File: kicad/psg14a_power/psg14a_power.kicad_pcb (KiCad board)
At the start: 2 copper layers, 12 parts, among them J1 Power, J2 In, J3 Out, Q1 IRF9Z24N

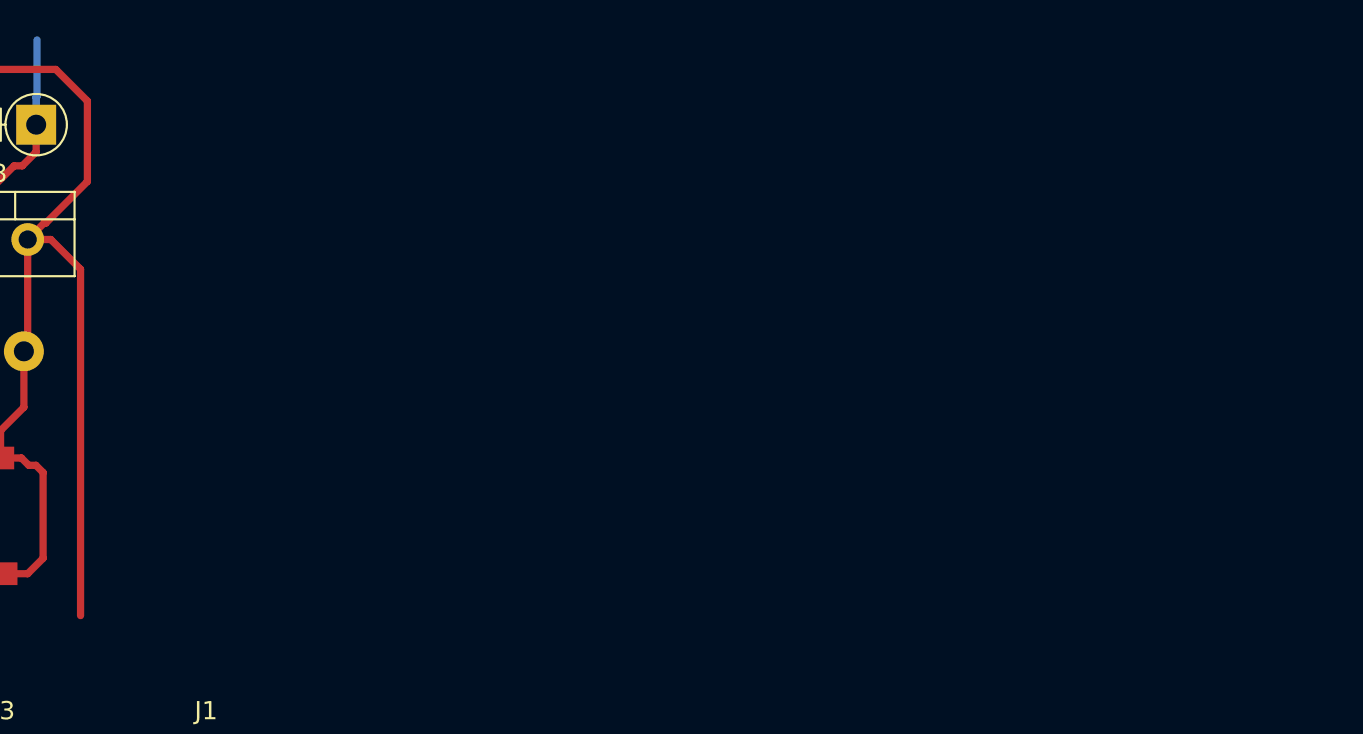
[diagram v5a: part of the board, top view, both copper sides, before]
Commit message: [psg14a_power] New layout
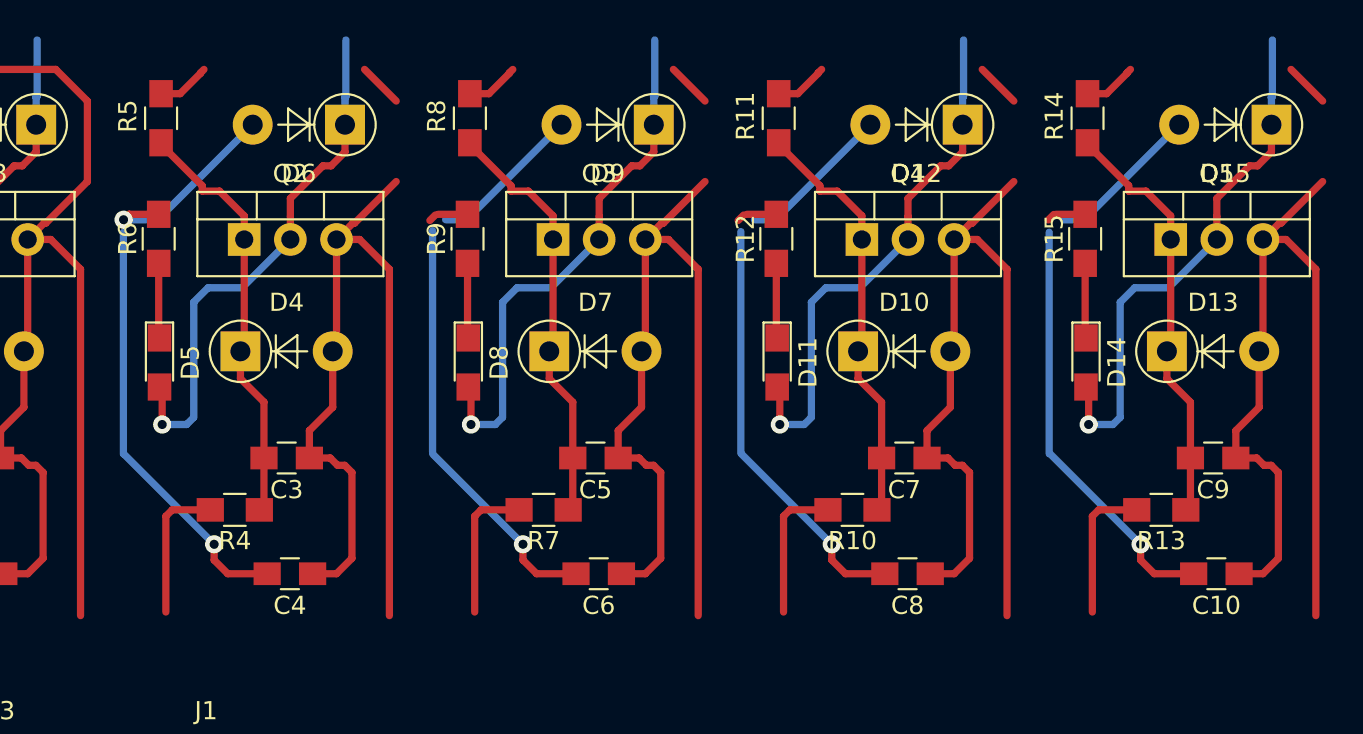
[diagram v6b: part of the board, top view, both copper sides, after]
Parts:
- added C10: 1uF 50V, Capacitors_SMD:C_0805_HandSoldering, F.Cu at (102.6, 56.2)
- added C3: 10nF, Capacitors_SMD:C_0805_HandSoldering, F.Cu at (51.4, 49.8)
- added C4: 1uF 50V, Capacitors_SMD:C_0805_HandSoldering, F.Cu at (51.6, 56.2)
- added C5: 10nF, Capacitors_SMD:C_0805_HandSoldering, F.Cu at (68.4, 49.8)
- added C6: 1uF 50V, Capacitors_SMD:C_0805_HandSoldering, F.Cu at (68.6, 56.2)
- added C7: 10nF, Capacitors_SMD:C_0805_HandSoldering, F.Cu at (85.4, 49.8)
- added C8: 1uF 50V, Capacitors_SMD:C_0805_HandSoldering, F.Cu at (85.6, 56.2)
- added C9: 10nF, Capacitors_SMD:C_0805_HandSoldering, F.Cu at (102.4, 49.8)
- added D10: BZX85_C12, Diodes_THT:D_DO-41_SOD81_P5.08mm_Vertical_AnodeUp, F.Cu at (82.8, 43.9)
- added D11: green, LEDs:LED_0805_HandSoldering, F.Cu at (78.4, 44.6)
- added D12: UF4007, Diodes_THT:D_DO-41_SOD81_P5.08mm_Vertical_AnodeUp, F.Cu at (88.6, 31.5)
- added D13: BZX85_C12, Diodes_THT:D_DO-41_SOD81_P5.08mm_Vertical_AnodeUp, F.Cu at (99.8, 43.9)
- added D14: green, LEDs:LED_0805_HandSoldering, F.Cu at (95.4, 44.6)
- added D15: UF4007, Diodes_THT:D_DO-41_SOD81_P5.08mm_Vertical_AnodeUp, F.Cu at (105.6, 31.5)
- added D4: BZX85_C12, Diodes_THT:D_DO-41_SOD81_P5.08mm_Vertical_AnodeUp, F.Cu at (48.8, 43.9)
- added D5: green, LEDs:LED_0805_HandSoldering, F.Cu at (44.4, 44.6)
- added D6: UF4007, Diodes_THT:D_DO-41_SOD81_P5.08mm_Vertical_AnodeUp, F.Cu at (54.6, 31.5)
- added D7: BZX85_C12, Diodes_THT:D_DO-41_SOD81_P5.08mm_Vertical_AnodeUp, F.Cu at (65.8, 43.9)
- added D8: green, LEDs:LED_0805_HandSoldering, F.Cu at (61.4, 44.6)
- added D9: UF4007, Diodes_THT:D_DO-41_SOD81_P5.08mm_Vertical_AnodeUp, F.Cu at (71.6, 31.5)
- added Q2: IRF9Z24N, TO_SOT_Packages_THT:TO-220-3_Vertical, F.Cu at (49.0, 37.8)
- added Q3: IRF9Z24N, TO_SOT_Packages_THT:TO-220-3_Vertical, F.Cu at (66.0, 37.8)
- added Q4: IRF9Z24N, TO_SOT_Packages_THT:TO-220-3_Vertical, F.Cu at (83.0, 37.8)
- added Q5: IRF9Z24N, TO_SOT_Packages_THT:TO-220-3_Vertical, F.Cu at (100.0, 37.8)
- added R10: 10K, Resistors_SMD:R_0805_HandSoldering, F.Cu at (82.5, 52.7)
- added R11: 10K, Resistors_SMD:R_0805_HandSoldering, F.Cu at (78.5, 31.1)
- added R12: 5k1, Resistors_SMD:R_0805_HandSoldering, F.Cu at (78.3, 37.7)
- added R13: 10K, Resistors_SMD:R_0805_HandSoldering, F.Cu at (99.5, 52.7)
- added R14: 10K, Resistors_SMD:R_0805_HandSoldering, F.Cu at (95.5, 31.1)
- added R15: 5k1, Resistors_SMD:R_0805_HandSoldering, F.Cu at (95.3, 37.7)
- added R4: 10K, Resistors_SMD:R_0805_HandSoldering, F.Cu at (48.5, 52.7)
- added R5: 10K, Resistors_SMD:R_0805_HandSoldering, F.Cu at (44.5, 31.1)
- added R6: 5k1, Resistors_SMD:R_0805_HandSoldering, F.Cu at (44.3, 37.7)
- added R7: 10K, Resistors_SMD:R_0805_HandSoldering, F.Cu at (65.5, 52.7)
- added R8: 10K, Resistors_SMD:R_0805_HandSoldering, F.Cu at (61.5, 31.1)
- added R9: 5k1, Resistors_SMD:R_0805_HandSoldering, F.Cu at (61.3, 37.7)
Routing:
- net /+24V: track 68.5 -> 289.4 mm
- net /GND: track 35.3 -> 171.7 mm, vias 2 -> 7
- net /Out3: track 0.00 -> 29.7 mm, vias 0 -> 1
- net /Out5: track 0.00 -> 29.7 mm, vias 0 -> 1
- net /Out4: track 0.00 -> 29.7 mm, vias 0 -> 1
- net /Out2: track 0.00 -> 29.7 mm, vias 0 -> 1
- net Net-(C3-Pad2): track 0.00 -> 23.4 mm
- net Net-(C9-Pad2): track 0.00 -> 23.4 mm
- net Net-(C7-Pad2): track 0.00 -> 23.4 mm
- net Net-(C5-Pad2): track 0.00 -> 23.4 mm
- net /In3: track 0.00 -> 7.86 mm
- net /In5: track 0.00 -> 7.86 mm
- net /In4: track 0.00 -> 7.86 mm
- net /In2: track 0.00 -> 7.86 mm
- net Net-(D14-Pad1): track 0.00 -> 4.13 mm
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
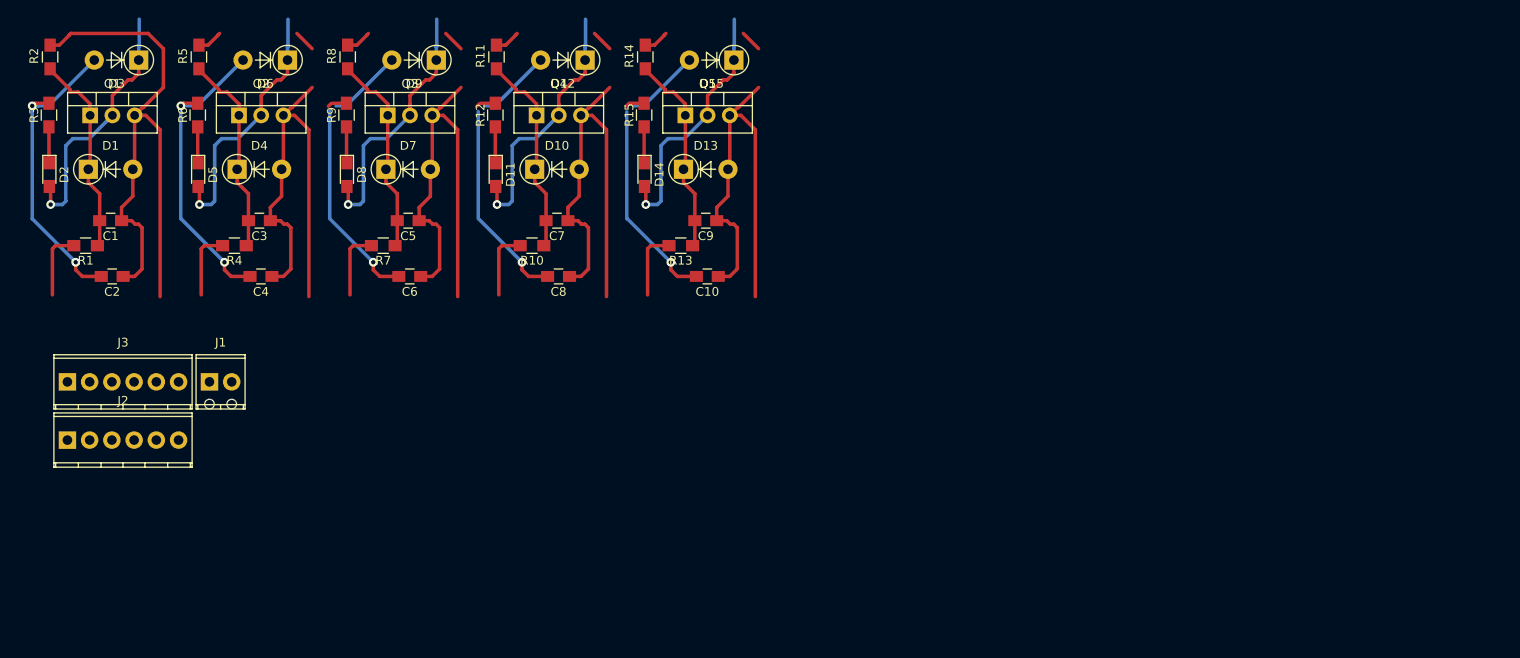
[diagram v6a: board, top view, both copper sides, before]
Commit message: [psg14a_power] New layout again
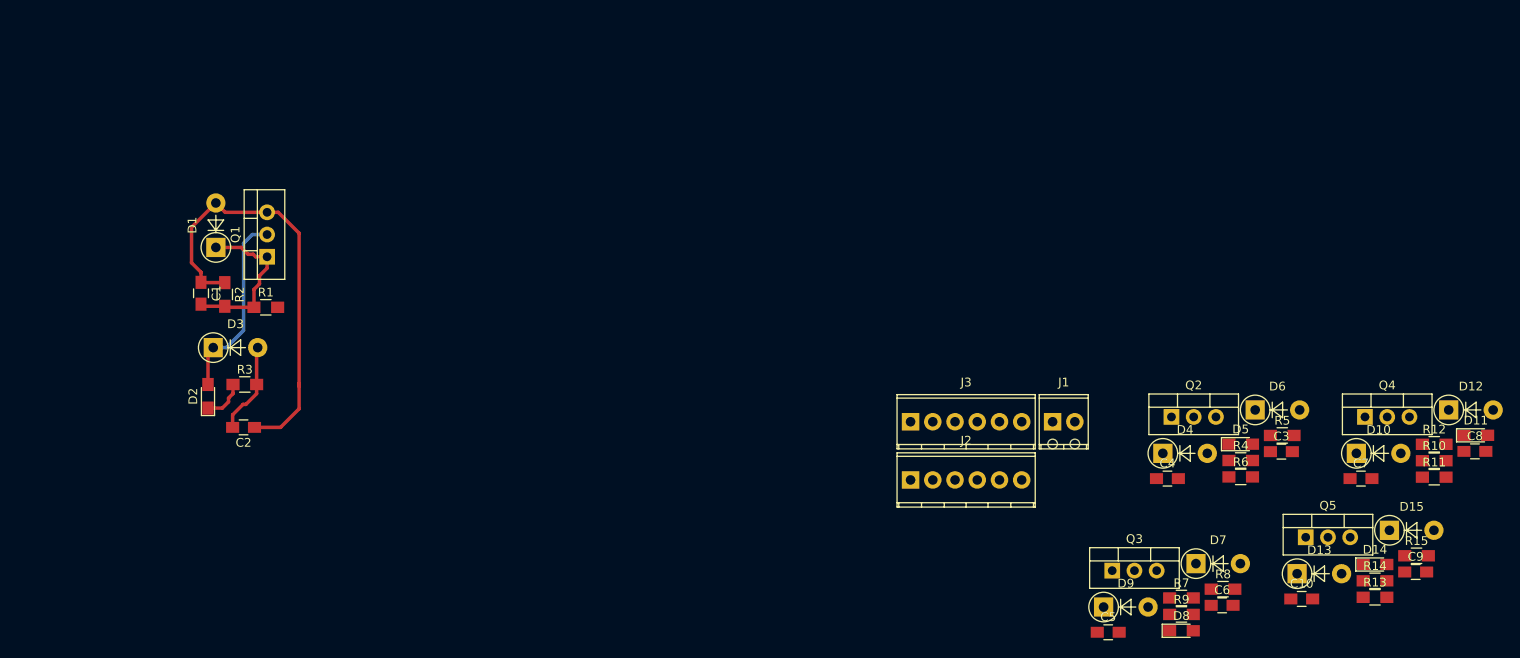
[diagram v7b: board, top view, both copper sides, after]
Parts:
- moved R5 131.1 mm to (168.3, 74.4), turned to 0 degrees
- moved R6 126.1 mm to (163.5, 79.1), turned to 0 degrees
- moved D5 123.0 mm to (163.5, 75.3), turned to 0 degrees
- moved C3 119.7 mm to (168.2, 76.2), turned to 0 degrees
- moved D6 117.6 mm to (165.2, 71.4), turned to 0 degrees
- moved R4 117.6 mm to (163.5, 77.2), turned to 0 degrees
- moved R11 117.4 mm to (185.6, 79.1), turned to 0 degrees
- moved R8 117.0 mm to (161.5, 91.9), turned to 0 degrees
- moved D11 115.9 mm to (190.4, 74.3), turned to 0 degrees
- moved R12 113.7 mm to (185.6, 75.4), turned to 0 degrees
- moved Q2 112.0 mm to (155.6, 72.2)
- moved R9 111.2 mm to (156.7, 94.8), turned to 0 degrees
- moved D4 110.6 mm to (154.6, 76.4)
- moved D8 108.7 mm to (156.7, 96.7), turned to 0 degrees
- moved C8 106.6 mm to (190.3, 76.2), turned to 0 degrees
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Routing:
- net /+24V: track 289.4 -> 50.7 mm
- net /GND: track 171.7 -> 10.5 mm, vias 7 -> 0
- net /Out3: track 29.7 -> 0.00 mm, vias 1 -> 0
- net /Out5: track 29.7 -> 0.00 mm, vias 1 -> 0
- net /Out4: track 29.7 -> 0.00 mm, vias 1 -> 0
- net /Out2: track 29.7 -> 0.00 mm, vias 1 -> 0
- net Net-(C3-Pad2): track 23.4 -> 0.00 mm
- net Net-(C9-Pad2): track 23.4 -> 0.00 mm
- net Net-(C7-Pad2): track 23.4 -> 0.00 mm
- net Net-(C5-Pad2): track 23.4 -> 0.00 mm
- net /In3: track 7.86 -> 0.00 mm
- net /In1: track 7.86 -> 0.00 mm
- net /In5: track 7.86 -> 0.00 mm
- net /In4: track 7.86 -> 0.00 mm
- net /In2: track 7.86 -> 0.00 mm
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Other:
- net class Default: clearance 0.25 -> 0.2
- rule pad_to_mask_clearance: 0.051 -> 0
- rule trace_clearance: 0.25 -> 0.2

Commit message: [psg14a_power] Routing in progress
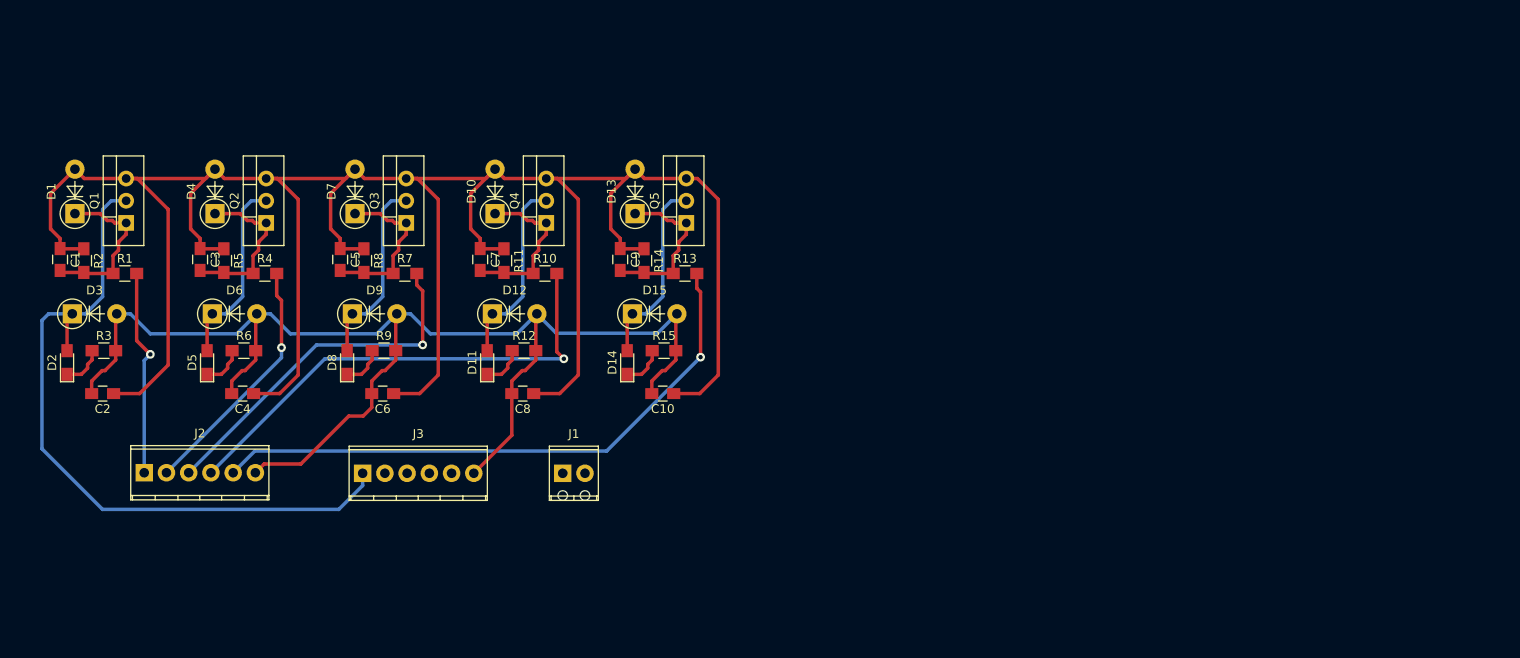
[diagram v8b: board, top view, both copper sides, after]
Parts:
- moved C3 125.5 mm to (44.6, 54.2), turned to 270 degrees
- moved R5 122.6 mm to (47.3, 54.4), turned to 270 degrees
- moved D6 119.7 mm to (46.0, 60.5)
- moved D5 118.5 mm to (45.4, 66.0), turned to 90 degrees
- moved R6 114.8 mm to (49.6, 64.7)
- moved R4 113.5 mm to (52.0, 55.8)
- moved D11 113.3 mm to (77.4, 66.0), turned to 90 degrees
- moved D4 111.7 mm to (46.3, 49.0), turned to 90 degrees
- moved D12 109.8 mm to (78.0, 60.5)
- moved R11 109.1 mm to (79.3, 54.4), turned to 270 degrees
- moved C8 109.0 mm to (81.5, 69.6), turned to 180 degrees
- moved C4 106.1 mm to (49.5, 69.6), turned to 180 degrees
- moved Q2 105.8 mm to (52.2, 50.1), turned to 90 degrees
- moved R8 105.1 mm to (63.3, 54.4), turned to 270 degrees
- moved R12 104.5 mm to (81.6, 64.7)
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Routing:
- net /+24V: track 50.7 -> 295.2 mm
- net /GND: track 10.5 -> 152.8 mm
- net /In5: track 0.00 -> 68.6 mm, vias 0 -> 1
- net /Out1: track 21.8 -> 82.3 mm
- net /In4: track 0.00 -> 55.8 mm, vias 0 -> 1
- net /In3: track 0.00 -> 41.2 mm, vias 0 -> 1
- net /In2: track 0.00 -> 28.4 mm, vias 0 -> 1
- net /In1: track 0.00 -> 23.7 mm, vias 0 -> 1
- net /Out5: track 0.00 -> 21.8 mm
- net /Out4: track 0.00 -> 21.8 mm
- net /Out3: track 0.00 -> 21.8 mm
- net /Out2: track 0.00 -> 21.8 mm
- net Net-(C5-Pad2): track 0.00 -> 18.9 mm
- net Net-(C3-Pad2): track 0.00 -> 18.9 mm
- net Net-(C9-Pad2): track 0.00 -> 18.9 mm
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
